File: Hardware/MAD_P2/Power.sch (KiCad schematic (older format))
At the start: 81 parts, among them J1 Line_3, J2 Line_1, J3 Line_2, J4 Power_In, U10 XL1509-ADJ, U11 APM4953, U12 APM4953, U2 XL1509-5.0, U3 XL1509-5.0, U4 XL1509-5.0, U5 XL1509-5.0, U6 XL1509-ADJ, U7 XL1509-ADJ, U8 XL1509-ADJ, U9 XL1509-ADJ

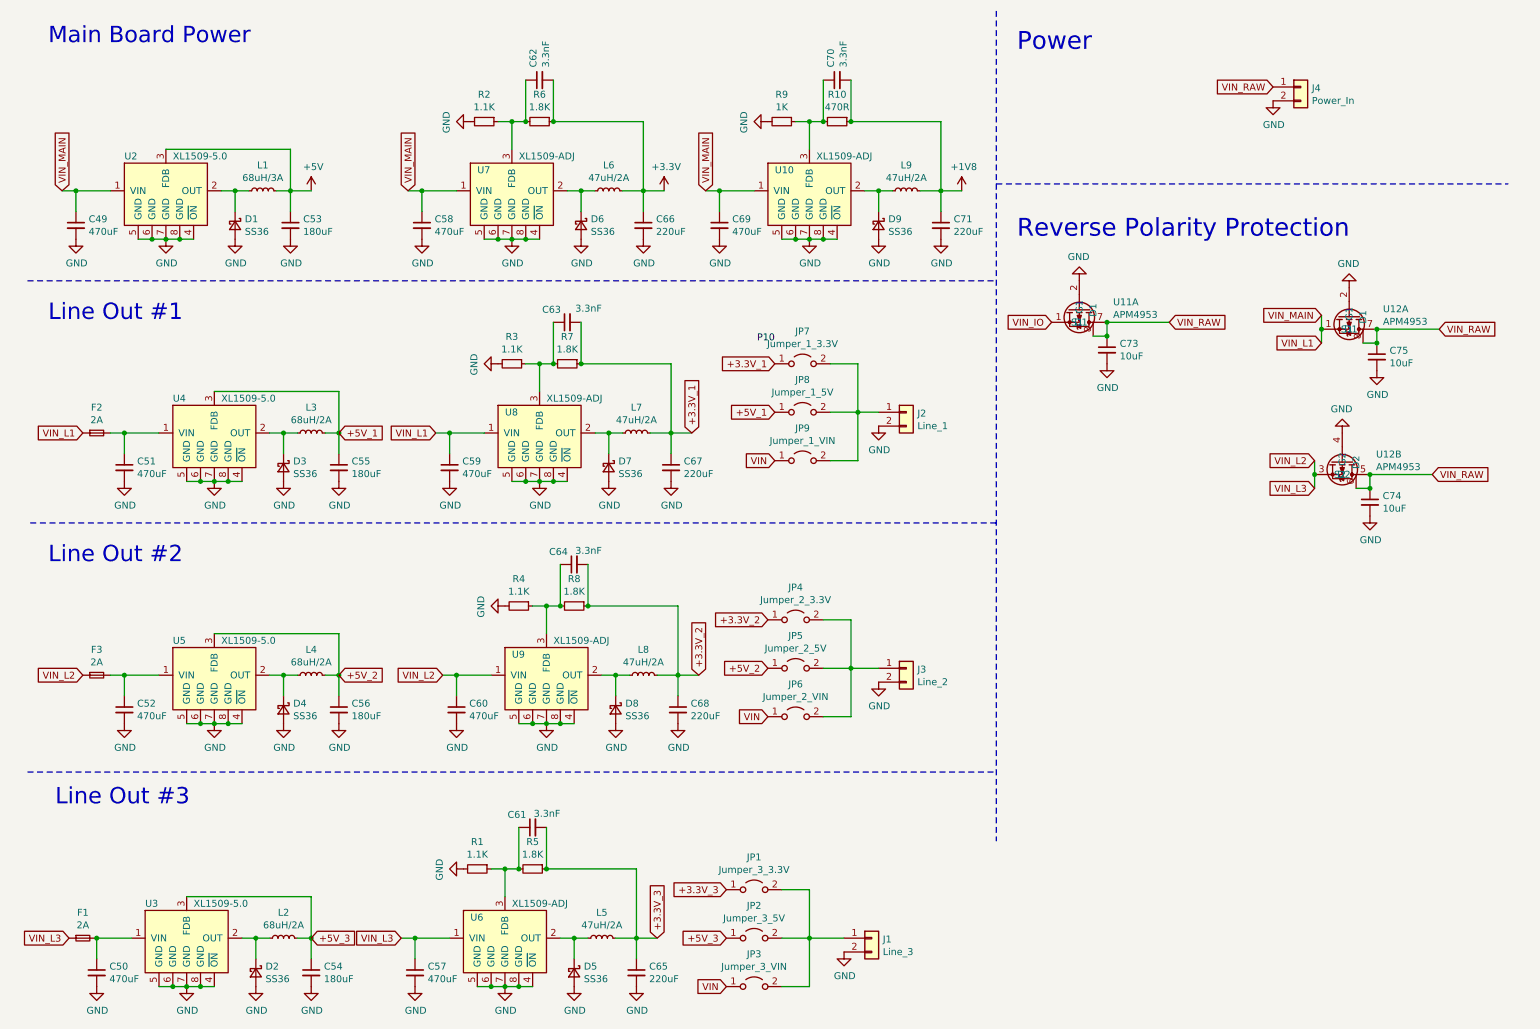
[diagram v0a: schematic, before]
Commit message: Added memory and usb to schematic
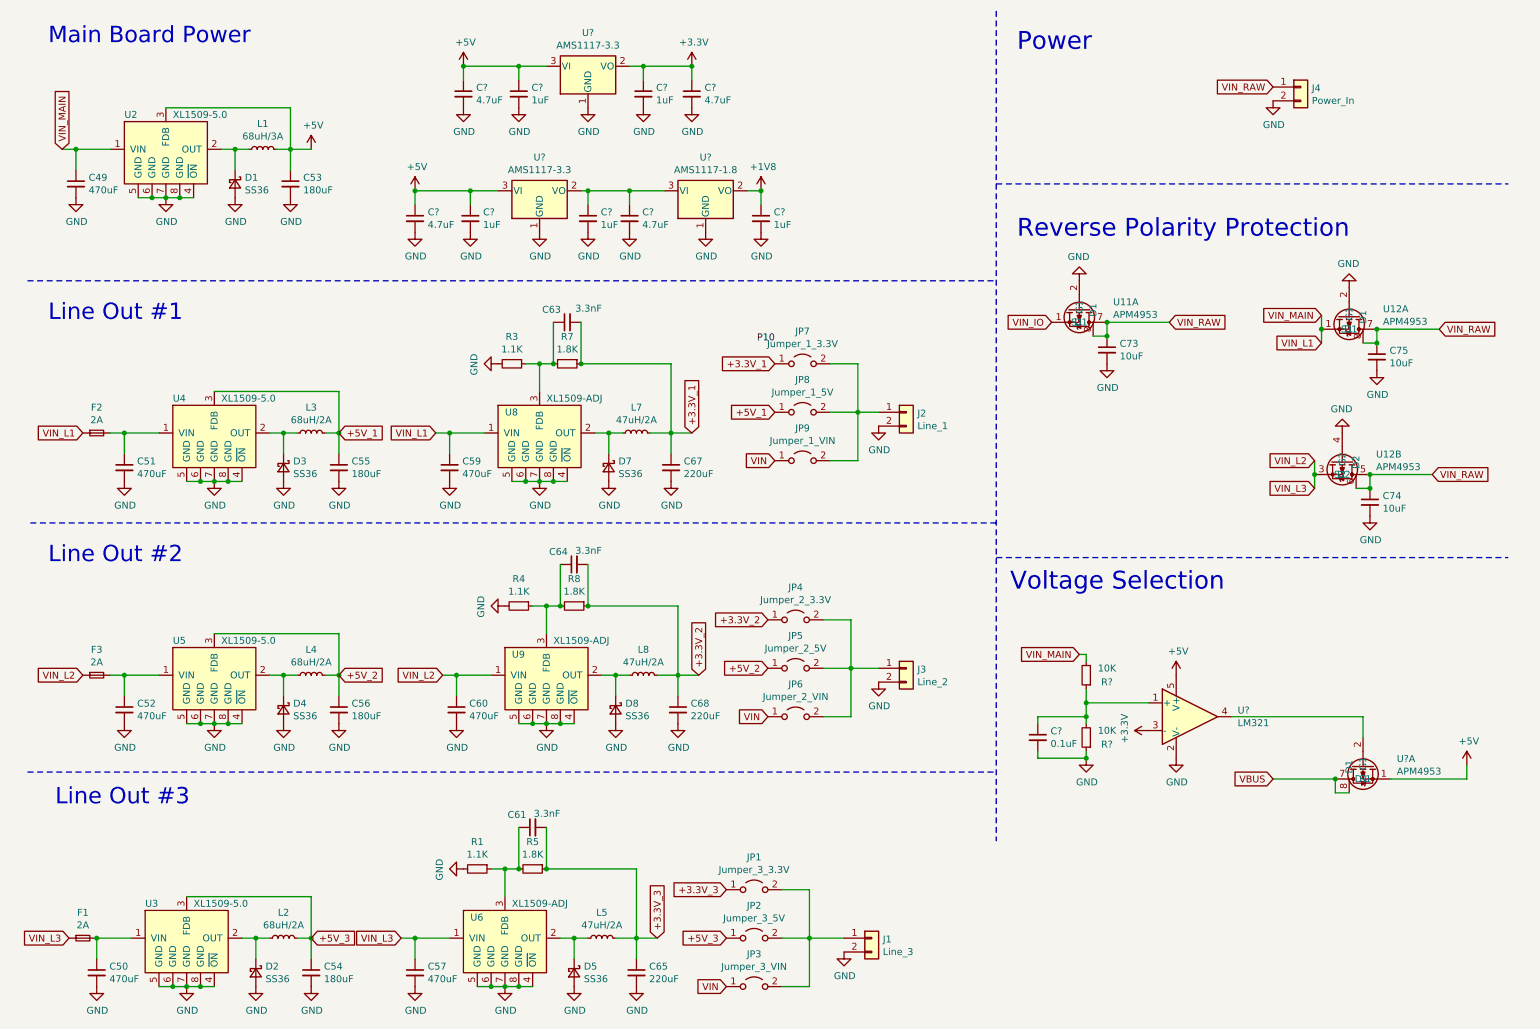
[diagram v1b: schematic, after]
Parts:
- removed C58, C69: 470uF, symbol Device:C_Small
- removed C62, C70: 3.3nF, symbol Device:C_Small
- removed C66, C71: 220uF, symbol Device:C_Small
- removed D6, D9: SS36, symbol Device:D_Schottky_Small
- removed L6, L9: 47uH/2A, symbol Device:L_Small
- removed R10: 470R, symbol Device:R_Small
- removed R2: 1.1K, symbol Device:R_Small
- removed R6: 1.8K, symbol Device:R_Small
- removed R9: 1K, symbol Device:R_Small
- removed U10, U7: XL1509-ADJ, symbol MAD_Board:XL1509
- added C?: 0.1uF, symbol Device:C_Small
- added C? (x5): 1uF, symbol Device:C_Small
- added C? (x4): 4.7uF, symbol Device:C_Small
- added R? (x2): 10K, symbol Device:R_Small
- added U?: LM321, Package_TO_SOT_SMD:SOT-23-5, symbol Amplifier_Operational:LM321
- added U?: APM4953, symbol MAD_Board:APM4953
- added U? (x2): AMS1117-3.3, Package_TO_SOT_SMD:SOT-223-3_TabPin2, symbol Regulator_Linear:AMS1117-3.3
- added U?: AMS1117-1.8, Package_TO_SOT_SMD:SOT-223-3_TabPin2, symbol Regulator_Linear:AMS1117-1.8
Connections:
- net +1V8: now also C?.1, U?.2 (VO)
- net +3V3: now also C?.1, C?.1, U?.2 (VO), U?.3 (-)
- net +5V: now also C?.1, C?.1, C?.1, C?.1, U?.1 (S1), U?.3 (VI), U?.3 (VI), U?.5 (V+)
- net GND: now also C?.2, C?.2, C?.2, C?.2, C?.2, C?.2, C?.2, C?.2, C?.2, C?.2, R?.1, U?.1 (GND), U?.1 (GND), U?.1 (GND), U?.2 (V-)
- net VIN_L1: now also R?.2
- new net: C?.1, R?.1, R?.2, U?.1 (+)
- new net: U?.2 (G1), U?.4
- new net: C?.1, C?.1, U?.2 (VO), U?.3 (VI)
- new net VBUS: U?.7 (D1), U?.8 (D1)
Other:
- note added: "Voltage Selection"
- moved on the sheet: C49, C53, D1, L1, U2

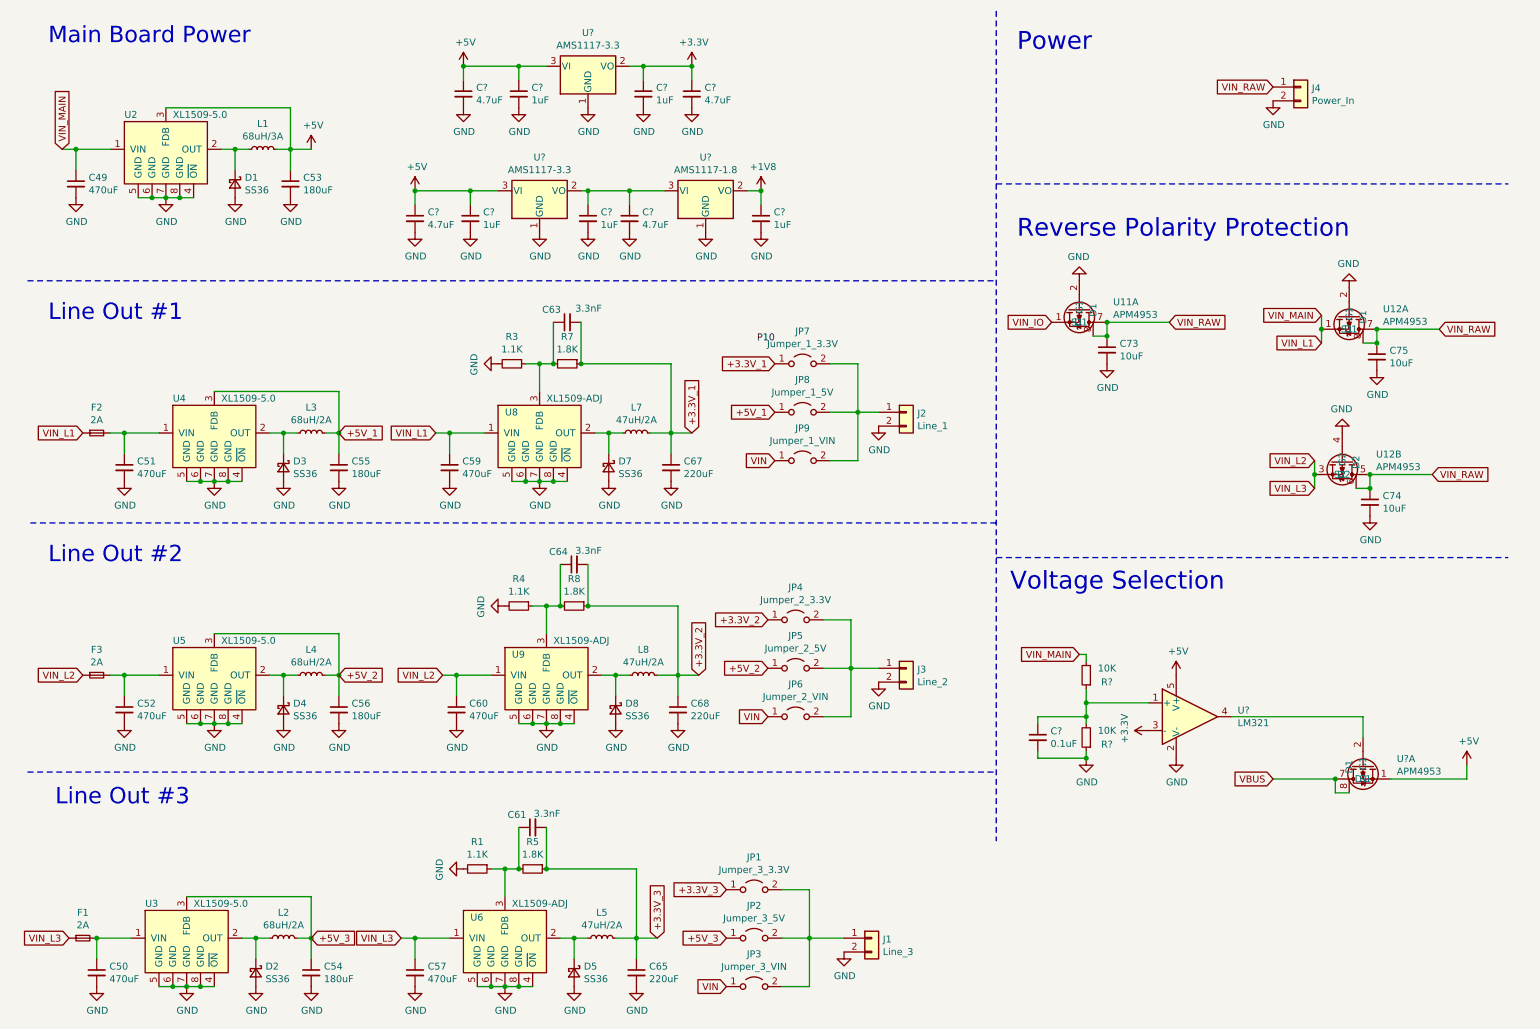
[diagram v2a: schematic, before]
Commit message: added adc
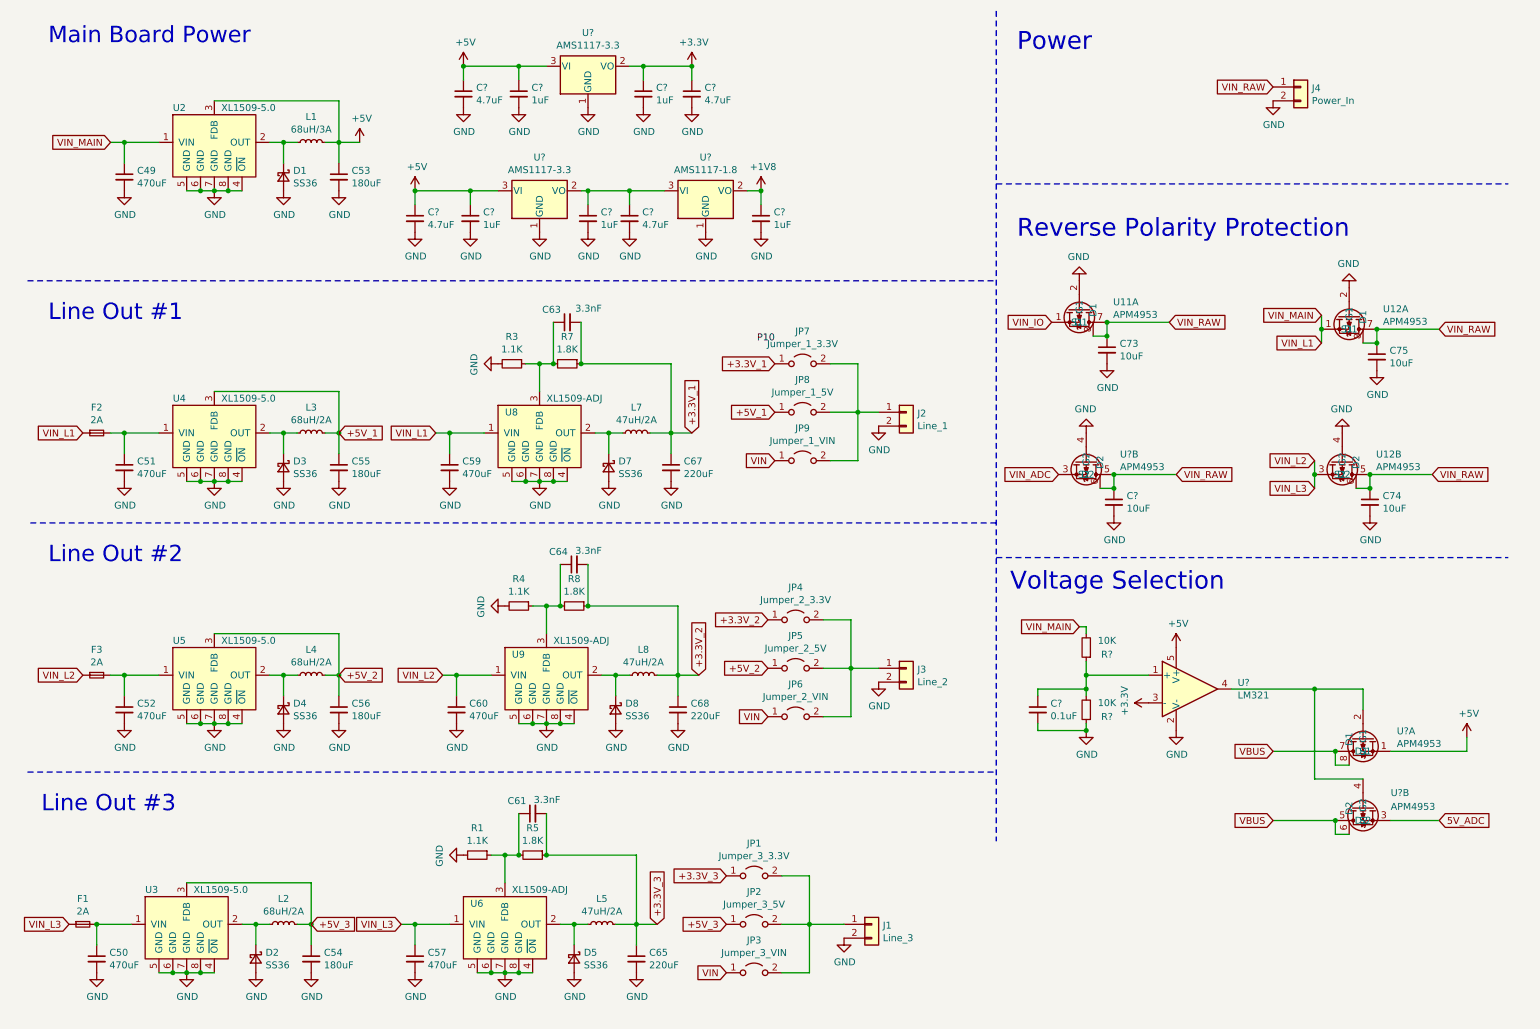
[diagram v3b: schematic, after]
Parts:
- added C?: 10uF, symbol Device:C_Small
- added U? (x2): APM4953, symbol MAD_Board:APM4953
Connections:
- net GND: now also C?.2, U?.4 (G2)
- net VBUS: now also U?.5 (D2), U?.6 (D2)
- net VIN_RAW: now also C?.1, U?.5 (D2), U?.6 (D2)
- net at U?.2 (G1), U?.4: now also U?.4 (G2)
- new net 5V_ADC: U?.3 (S2)
- new net VIN_ADC: U?.3 (S2)
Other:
- moved on the sheet: C49, C50, C53, C54, C57, C61, C65, C?, D1, D2, D5, F1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

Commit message: began pcb layout
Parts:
- removed D5, D7, D8: SS36, symbol Device:D_Schottky_Small
- removed L5, L7, L8: 47uH/2A, symbol Device:L_Small
- removed R1, R3, R4: 1.1K, symbol Device:R_Small
- removed R5, R7, R8: 1.8K, symbol Device:R_Small
- removed U6, U8, U9: XL1509-ADJ, symbol MAD_Board:XL1509
- added C140, C141, C142: 4.7uF, Capacitor_SMD:C_0603_1608Metric, symbol Device:C_Small
- added F5: 5A, MAD_P2:Wurth 696106003002 (15mm x 1.5mm), symbol Device:Fuse_Small
- added U6, U8, U9: AMS1117-3.3, Package_TO_SOT_SMD:SOT-223-3_TabPin2, symbol Regulator_Linear:AMS1117-3.3
- C49, C50, C51, C52: footprint (none) -> Capacitor_SMD:C_Elec_10x10.2
- C53, C54, C55, C56: footprint (none) -> Capacitor_SMD:C_Elec_6.3x7.7
- C57, C59, C60: value 470uF -> 4.7uF; footprint (none) -> Capacitor_SMD:C_0603_1608Metric
- C58, C62, C66, C69, C70, C71, C72, C88, C89, C90, C91: renamed from C?; footprint (none) -> Capacitor_SMD:C_0603_1608Metric
- C61, C63, C64: value 3.3nF -> 1uF; footprint (none) -> Capacitor_SMD:C_0603_1608Metric
- C65, C67, C68: value 220uF -> 1uF; footprint (none) -> Capacitor_SMD:C_0603_1608Metric
- C73, C74, C75: footprint (none) -> Capacitor_SMD:C_0603_1608Metric
- D1, D2, D3, D4: footprint (none) -> Diode_SMD:D_SMC
- F1, F2, F3: value 2A -> 5A; footprint (none) -> MAD_P2:Wurth 696106003002 (15mm x 1.5mm)
- J1, J2, J3, J4: footprint (none) -> Connector_AMASS:AMASS_XT30PW-M_1x02_P2.50mm_Horizontal
- JP1, JP2, JP3, JP4, JP5, JP6, JP7, JP8, JP9: footprint (none) -> Connector_PinHeader_2.54mm:PinHeader_1x02_P2.54mm_Vertical
- L1, L2, L3, L4: footprint (none) -> Inductor_SMD:L_10.4x10.4_H4.8
- R6, R9: renamed from R?; footprint (none) -> Resistor_SMD:R_0603_1608Metric
- U11, U21: renamed from U?; footprint (none) -> Package_SO:SOP-8_3.9x4.9mm_P1.27mm
- U11, U12, U2, U3, U4, U5: footprint (none) -> Package_SO:SOP-8_3.9x4.9mm_P1.27mm
- gave numbers to parts that had none: 4
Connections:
- net +3.3V_1: now also C141.1, U8.2 (VO); no longer C63.2
- net +3.3V_2: now also C142.1, U9.2 (VO); no longer C64.2
- net +3.3V_3: now also C140.1, U6.2 (VO); no longer C61.2
- net +5V_1: now also C59.1, C63.1, U8.3 (VI)
- net +5V_2: now also C60.1, C64.1, U9.3 (VI)
- net +5V_3: now also C57.1, C61.1, U6.3 (VI)
- net GND: now also C61.2, C63.2, C64.2, C140.2, C141.2, C142.2, U6.1 (GND), U8.1 (GND), U9.1 (GND)
- net VIN_L1: now also C51.1, U4.1 (VIN); no longer C59.1, F2.1
- net VIN_L2: now also C50.1, C52.1, U3.1 (VIN), U5.1 (VIN); no longer C57.1, C60.1, F1.1, F3.1
- net VIN_RAW: now also F1.2, F2.2, F3.2, F5.2; no longer C73.1, C74.1, C75.1, C91.1, U11.5 (D2), U11.6 (D2), U11.7 (D1), U11.8 (D1), U12.5 (D2), U12.6 (D2), U12.7 (D1), U12.8 (D1)
- new net: C91.1, F2.1, U11.5 (D2), U11.6 (D2)
- new net: C73.1, F1.1, U11.7 (D1), U11.8 (D1)
- new net: C74.1, F5.1, U12.5 (D2), U12.6 (D2)
- new net: C75.1, F3.1, U12.7 (D1), U12.8 (D1)
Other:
- note added: "Reverse Polarity and \nOver Current Protection"
- note removed: "Reverse Polarity Protection"
- moved on the sheet: C50, C51, C52, C54, C55, C56, C75, D2, D3, D4, L2, L3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

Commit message: finished board layout
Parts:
- removed F1, F2, F3, F5: 5A, MAD_P2:Wurth 696106003002 (15mm x 1.5mm), symbol Device:Fuse_Small
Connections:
- net VIN_RAW: now also C73.1, C74.1, C75.1, C91.1, U11.5 (D2), U11.6 (D2), U11.7 (D1), U11.8 (D1), U12.5 (D2), U12.6 (D2), U12.7 (D1), U12.8 (D1)
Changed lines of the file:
@@
 	1    0    0    -1
 $EndComp
-Text GLabel 10850 2800 2    50   Input ~ 0
+Text GLabel 10650 2800 2    50   Input ~ 0
 VIN_RAW
 Wire Wire Line
@@
 Text GLabel 9800 3750 0    50   Input ~ 0
 VIN_L2
-Text GLabel 8950 2750 2    50   Input ~ 0
+Text GLabel 8750 2750 2    50   Input ~ 0
 VIN_RAW
 Wire Wire Line
@@
 $EndComp
 Connection ~ 10200 3850
-Text GLabel 10850 3850 2    50   Input ~ 0
+Text GLabel 10650 3850 2    50   Input ~ 0
 VIN_RAW
 $Comp
@@
 Text GLabel 7950 3850 0    50   Input ~ 0
 VIN_ADC
-Text GLabel 9000 3850 2    50   Input ~ 0
+Text GLabel 8800 3850 2    50   Input ~ 0
 VIN_RAW
 Connection ~ 8350 3850
@@
 	900  3350 1200 3350
 $Comp
-L Device:Fuse_Small F1
-U 1 1 60DA25BC
-P 8850 2750
-F 0 "F1" H 8850 2935 50  0000 C CNN
-F 1 "5A" H 8850 2844 50  0000 C CNN
-F 2 "MAD_P2:Wurth 696106003002 (15mm x 1.5mm)" H 8850 2750 50  0001 C CNN
-F 3 "~" H 8850 2750 50  0001 C CNN
-	1    8850 2750
-	1    0    0    -1
-$EndComp
-$Comp
-L Device:Fuse_Small F2
-U 1 1 60DABDF0
-P 8900 3850
-F 0 "F2" H 8900 4035 50  0000 C CNN
-F 1 "5A" H 8900 3944 50  0000 C CNN
-F 2 "MAD_P2:Wurth 696106003002 (15mm x 1.5mm)" H 8900 3850 50  0001 C CNN
-F 3 "~" H 8900 3850 50  0001 C CNN
-	1    8900 3850
-	1    0    0    -1
-$EndComp
-$Comp
-L Device:Fuse_Small F5
-U 1 1 60DAC8FE
-P 10750 3850
-F 0 "F5" H 10750 4035 50  0000 C CNN
-F 1 "5A" H 10750 3944 50  0000 C CNN
-F 2 "MAD_P2:Wurth 696106003002 (15mm x 1.5mm)" H 10750 3850 50  0001 C CNN
-F 3 "~" H 10750 3850 50  0001 C CNN
-	1    10750 3850
-	1    0    0    -1
-$EndComp
-$Comp
-L Device:Fuse_Small F3
-U 1 1 60DADAD3
-P 10750 2800
-F 0 "F3" H 10750 2985 50  0000 C CNN
-F 1 "5A" H 10750 2894 50  0000 C CNN
-F 2 "MAD_P2:Wurth 696106003002 (15mm x 1.5mm)" H 10750 2800 50  0001 C CNN
-F 3 "~" H 10750 2800 50  0001 C CNN
-	1    10750 2800
-	1    0    0    -1
-$EndComp
-$Comp
 L Regulator_Linear:AMS1117-3.3 U8
